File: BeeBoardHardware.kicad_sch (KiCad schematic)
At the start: 48 parts, among them J1 Conn_01x10, J2 USB_C_Receptacle_USB2.0_16P, J3 Conn_01x02, Q1 AO3413, Q2 MMBT3904, Q3 MMBT3904, SW1 SW_Push, U1 MCP16311x-xMNY, U2 BQ24074RGT, U3 USBLC6-2SC6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

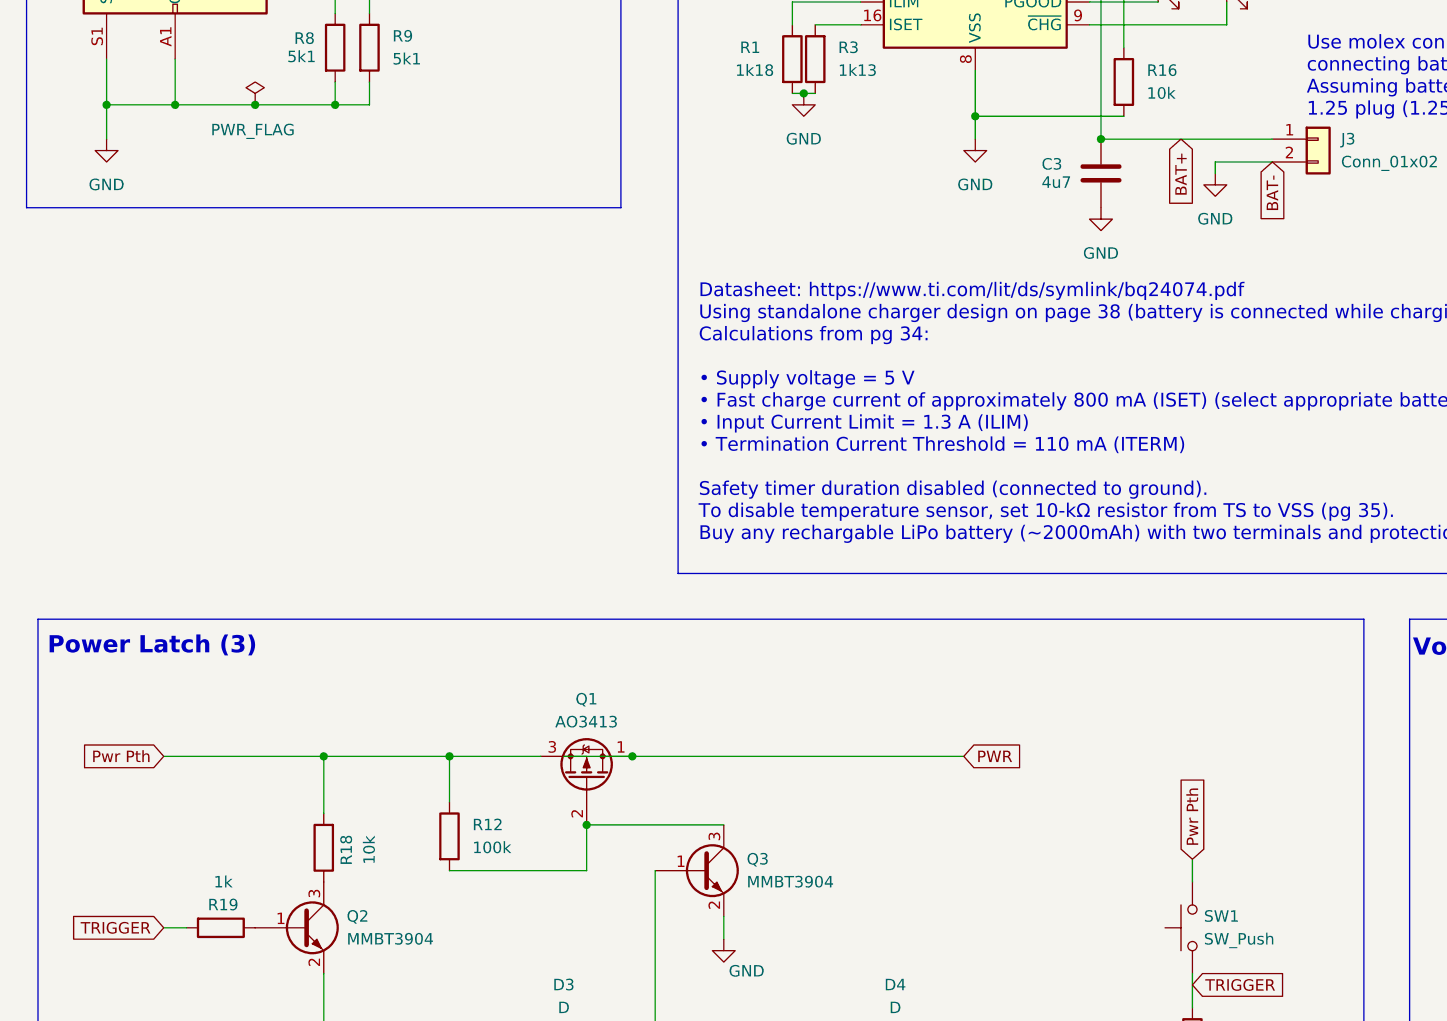
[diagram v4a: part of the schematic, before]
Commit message: updated stepper files
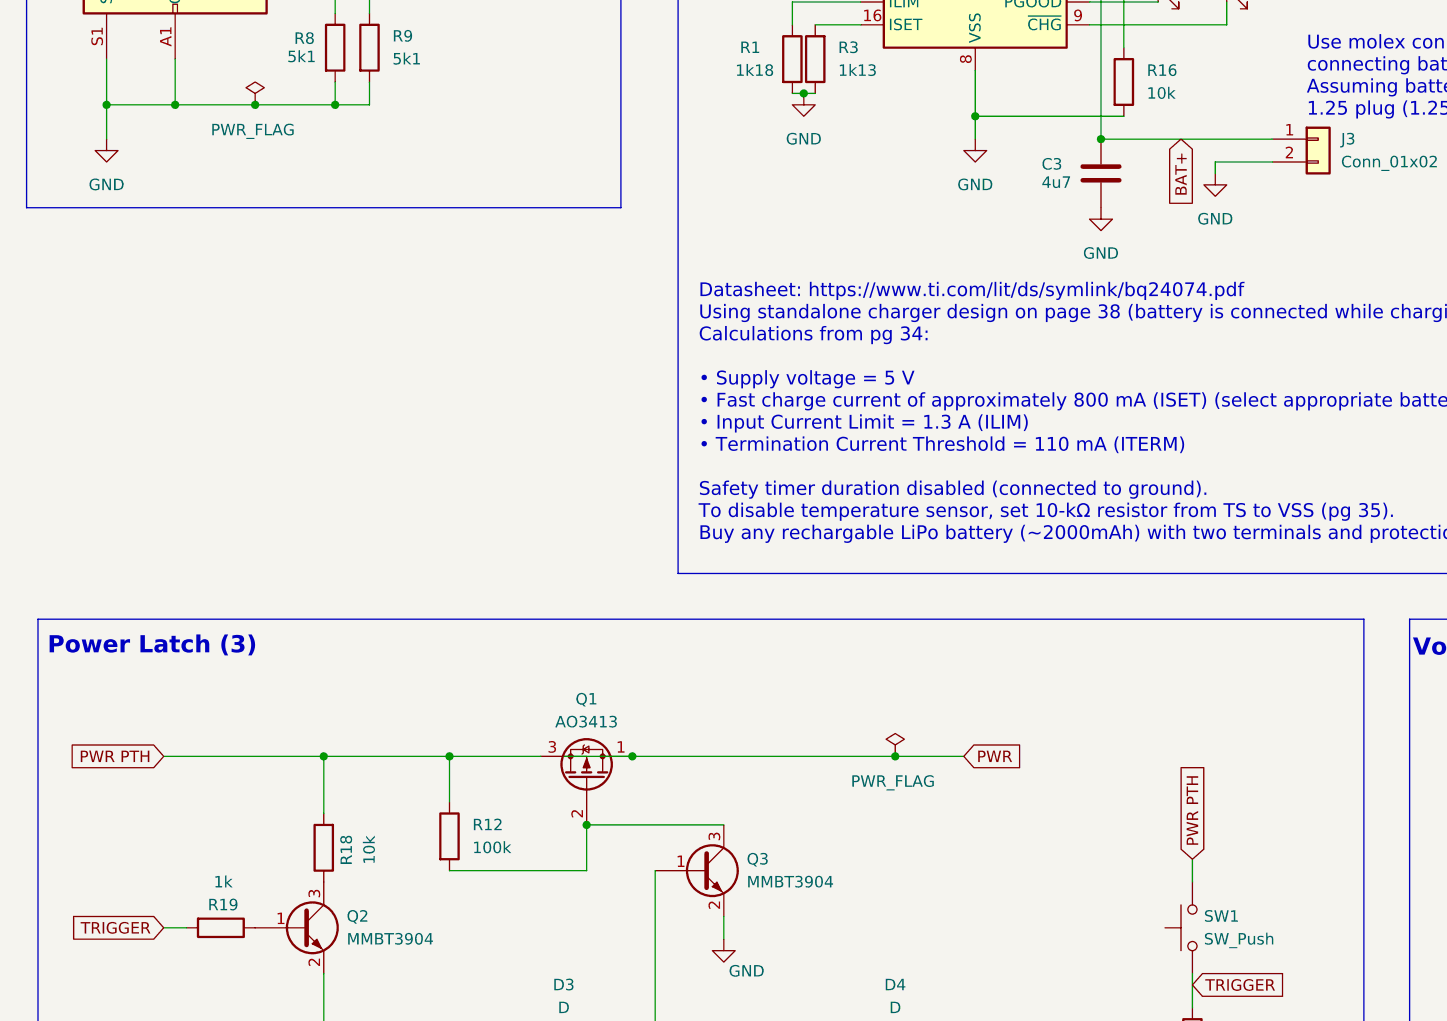
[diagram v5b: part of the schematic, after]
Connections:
- net Pwr Pth is gone; now on net PWR PTH: Q1.3 (S), R12.1, R18.2, SW1.2
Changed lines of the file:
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@@
 	)
 	(junction
+		(at 118.11 148.59)
+		(diameter 0)
+		(color 0 0 0 0)
+	)
+	(junction
 		(at 232.41 153.67)
 		(diameter 0)
@@
 	(wire
 		(pts
-			(xy 88.9 148.59) (xy 125.73 148.59)
+			(xy 88.9 148.59) (xy 118.11 148.59)
 		)
 		(stroke
@@
 	(wire
 		(pts
+			(xy 118.11 148.59) (xy 125.73 148.59)
+		)
+		(stroke
+			(width 0)
+			(type default)
+		)
+	)
+	(wire
+		(pts
 			(xy 55.88 73.66) (xy 55.88 76.2)
 		)
@@
 		)
 	)
-	(global_label "Pwr Pth"
+	(global_label "PWR PTH"
 		(shape input)
 		(at 36.83 148.59 180)
@@
 		)
 		(property "Intersheetrefs" "${INTERSHEET_REFS}"
-			(at 26.3458 148.59 0)
+			(at 25.3177 148.59 0)
 			(effects
 				(font
@@
 		)
 	)
-	(global_label "BAT-"
-		(shape input)
-		(at 160.02 82.55 270)
-		(fields_autoplaced yes)
-		(effects
-			(font
-				(size 1.27 1.27)
-			)
-			(justify right)
-		)
-		(property "Intersheetrefs" "${INTERSHEET_REFS}"
-			(at 160.02 90.4338 90)
-			(effects
-				(font
-					(size 1.27 1.27)
-				)
-				(justify right)
-				(hide yes)
-			)
-		)
-	)
 	(global_label "TRIGGER"
 		(shape input)
@@
 		)
 	)
-	(global_label "Pwr Pth"
+	(global_label "PWR PTH"
 		(shape input)
 		(at 151.13 160.02 90)
@@
 		)
 		(property "Intersheetrefs" "${INTERSHEET_REFS}"
-			(at 151.13 149.5358 90)
+			(at 151.13 148.5077 90)
 			(effects
 				(font
@@
 					(unit 1)
 				)
+			)
+		)
+	)
+	(symbol
+		(lib_id "power:PWR_FLAG")
+		(at 118.11 148.59 0)
+		(unit 1)
+		(exclude_from_sim no)
+		(in_bom yes)
+		(on_board yes)
+		(dnp no)
+		(property "Reference" "#FLG03"
+			(at 118.11 146.685 0)
+			(effects
+				(font
+					(size 1.27 1.27)
+				)
+				(hide yes)
+			)
+		)
+		(property "Value" "PWR_FLAG"
+			(at 117.856 151.384 0)
+			(effects
+				(font
+					(size 1.27 1.27)
+				)
+			)
+		)
+		(property "Footprint" ""
+			(at 118.11 148.59 0)
+			(effects
+				(font
+					(size 1.27 1.27)
+				)
+				(hide yes)
+			)
+		)
+		(property "Datasheet" "~"
+			(at 118.11 148.59 0)
+			(effects
+				(font
+					(size 1.27 1.27)
+				)
+				(hide yes)
+			)
+		)
+		(property "Description" "Special symbol for telling ERC where power comes from"
+			(at 118.11 148.59 0)
+			(effects
+				(font
+					(size 1.27 1.27)
+				)
+				(hide yes)
+			)
+		)
+		(pin "1"
+		)
+		(instances
+			(project "BeeBoardHardware"
+				(path "/e994c545-1735-4419-a83b-30b4b610da30"
+					(reference "#FLG03")
+					(unit 1)
+				)

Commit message: organized pcb
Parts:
- removed Q1: AO3413, Package_TO_SOT_SMD:SOT-23, symbol Device:Q_PMOS_DGS
- added Q4: AO3413, Package_TO_SOT_SMD:SOT-23, symbol Device:Q_PMOS_GSD
- added R21: 1k, Resistor_SMD:R_0402_1005Metric, symbol Device:R
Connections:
- net +3v3: now also R21.1
- net GND: now also R21.2
- net PWR: now also Q4.2 (S)
- net PWR PTH: now also Q4.3 (D)
- net at Q3.3 (C), R12.2: now also Q4.1 (G)
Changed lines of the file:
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@@
 	)
 	(junction
-		(at 83.82 156.21)
-		(diameter 0)
-		(color 0 0 0 0)
-	)
-	(junction
 		(at 204.47 151.13)
 		(diameter 0)
@@
 	)
 	(junction
-		(at 101.6 54.61)
+		(at 83.82 156.21)
 		(diameter 0)
 		(color 0 0 0 0)
 	)
 	(junction
-		(at 62.23 33.02)
+		(at 101.6 54.61)
 		(diameter 0)
 		(color 0 0 0 0)
 	)
 	(junction
-		(at 248.92 67.31)
+		(at 62.23 33.02)
 		(diameter 0)
 		(color 0 0 0 0)
 	)
 	(junction
-		(at 54.61 148.59)
+		(at 248.92 67.31)
 		(diameter 0)
 		(color 0 0 0 0)
 	)
 	(junction
-		(at 88.9 148.59)
+		(at 54.61 148.59)
 		(diameter 0)
 		(color 0 0 0 0)
@@
 	(wire
 		(pts
-			(xy 81.28 148.59) (xy 88.9 148.59)
-		)
-		(stroke
-			(width 0)
-			(type default)
-		)
-	)
-	(wire
-		(pts
 			(xy 193.04 151.13) (xy 204.47 151.13)
 		)
@@
 		)
 	)
+	(global_label "+3v3"
+		(shape input)
+		(at 281.94 153.67 90)
+		(fields_autoplaced yes)
+		(effects
+			(font
+				(size 1.27 1.27)
+			)
+			(justify left)
+		)
+		(property "Intersheetrefs" "${INTERSHEET_REFS}"
+			(at 281.94 145.7258 90)
+			(effects
+				(font
+					(size 1.27 1.27)
+				)
+				(justify left)
+				(hide yes)
+			)
+		)
+	)
 	(symbol
 		(lib_id "Device:D")
@@
 	)
 	(symbol
+		(lib_id "power:GND")
+		(at 281.94 161.29 0)
+		(unit 1)
+		(exclude_from_sim no)
+		(in_bom yes)
+		(on_board yes)
+		(dnp no)
+		(property "Reference" "#PWR09"
+			(at 281.94 167.64 0)
+			(effects
+				(font
+					(size 1.27 1.27)
+				)
+				(hide yes)
+			)
+		)
+		(property "Value" "GND"
+			(at 281.94 166.37 0)
+			(effects
+				(font
+					(size 1.27 1.27)
+				)
+			)
+		)
+		(property "Footprint" ""
+			(at 281.94 161.29 0)
+			(effects
+				(font
+					(size 1.27 1.27)
+				)
+				(hide yes)
+			)
+		)
+		(property "Datasheet" ""
+			(at 281.94 161.29 0)
+			(effects
+				(font
+					(size 1.27 1.27)
+				)
+				(hide yes)
+			)
+		)
+		(property "Description" "Power symbol creates a global label with name \"GND\" , ground"
+			(at 281.94 161.29 0)
+			(effects
+				(font
+					(size 1.27 1.27)
+				)
+				(hide yes)
+			)
+		)
+		(pin "1"
+		)
+		(instances
+			(project "BeeBoardHardware"
+				(path "/e994c545-1735-4419-a83b-30b4b610da30"
+					(reference "#PWR09")
+					(unit 1)
+				)
+			)
+		)
+	)
+	(symbol
 		(lib_id "Device:C")
 		(at 120.65 31.75 0)
@@
 	)
 	(symbol
+		(lib_id "Device:R")
+		(at 281.94 157.48 0)
+		(unit 1)
+		(exclude_from_sim no)
+		(in_bom yes)
+		(on_board yes)
+		(dnp no)
+		(property "Reference" "R21"
+			(at 279.4 157.226 90)
+			(effects
+				(font
+					(size 1.27 1.27)
+				)
+			)
+		)
+		(property "Value" "1k"
+			(at 276.86 157.226 90)
+			(effects
+				(font
+					(size 1.27 1.27)
+				)
+			)
+		)
+		(property "Footprint" "Resistor_SMD:R_0402_1005Metric"
+			(at 280.162 157.48 90)
+			(effects
+				(font
+					(size 1.27 1.27)
+				)
+				(hide yes)
+			)
+		)
+		(property "Datasheet" "~"
+			(at 281.94 157.48 0)
+			(effects
+				(font
+					(size 1.27 1.27)
+				)
+				(hide yes)
+			)
+		)
+		(property "Description" "Resistor"
+			(at 281.94 157.48 0)
+			(effects
+				(font
+					(size 1.27 1.27)
+				)
+				(hide yes)
+			)
+		)
+		(property "Digikey Link" ""
+			(at 281.94 157.48 0)
+			(effects
+				(font
+					(size 1.27 1.27)
+				)
+				(hide yes)
+			)
+		)
+		(property "Manufacturer Product Number" ""
+			(at 281.94 157.48 0)
+			(effects
+				(font
+					(size 1.27 1.27)
+				)
+				(hide yes)
+			)
+		)
+		(pin "1"
+		)
+		(pin "2"
+		)
+		(instances
+			(project "BeeBoardHardware"
+				(path "/e994c545-1735-4419-a83b-30b4b610da30"
+					(reference "R21")
+					(unit 1)
+				)
+			)
+		)
+	)
+	(symbol
 		(lib_id "Device:C")
 		(at 163.83 50.8 0)
@@
 	)
 	(symbol
-		(lib_id "Device:Q_PMOS_DGS")
-		(at 83.82 151.13 270)
-		(mirror x)
-		(unit 1)
-		(exclude_from_sim no)
-		(in_bom yes)
-		(on_board yes)
-		(dnp no)
-		(property "Reference" "Q1"
-			(at 83.82 142.24 90)
-			(effects
-				(font
-					(size 1.27 1.27)
-				)
-			)
-		)
-		(property "Value" "AO3413"
-			(at 83.82 144.78 90)
-			(effects
-				(font
-					(size 1.27 1.27)
-				)
-			)
-		)
-		(property "Footprint" "Package_TO_SOT_SMD:SOT-23"
-			(at 86.36 146.05 0)
-			(effects
-				(font
-					(size 1.27 1.27)
-				)
-				(hide yes)
-			)
-		)
-		(property "Datasheet" "https://www.aosmd.com/sites/default/files/res/datasheets/AO3413.pdf"
-			(at 83.82 151.13 0)
-			(effects
-				(font
-					(size 1.27 1.27)
-				)
-				(hide yes)
-			)
-		)
-		(property "Description" "P-MOSFET transistor, drain/gate/source"
-			(at 83.82 151.13 0)
-			(effects
-				(font
-					(size 1.27 1.27)
-				)
-				(hide yes)
-			)
-		)
-		(property "Digikey Link" "https://www.digikey.com/en/products/detail/alpha-omega-semiconductor-inc/AO3413/1855780"
-			(at 83.82 151.13 0)
-			(effects
-				(font
-					(size 1.27 1.27)
-				)
-				(hide yes)
-			)
-		)
-		(property "Manufacturer Product Number" "AO3413"
-			(at 83.82 151.13 0)
-			(effects
-				(font
-					(size 1.27 1.27)
-				)
-				(hide yes)
-			)
-		)
-		(pin "1"
-		)
-		(pin "2"
-		)
-		(pin "3"
-		)
-		(instances
-			(project ""
-				(path "/e994c545-1735-4419-a83b-30b4b610da30"
-					(reference "Q1")
-					(unit 1)
-				)
-			)
-		)
-	)
-	(symbol
 		(lib_id "power:PWR_FLAG")
 		(at 46.99 76.2 0)
@@
 					(unit 1)
 				)
+			)
+		)
+	)
+	(symbol
+		(lib_id "Device:Q_PMOS_GSD")
+		(at 83.82 151.13 90)
+		(unit 1)
+		(exclude_from_sim no)
+		(in_bom yes)
+		(on_board yes)
+		(dnp no)
+		(fields_autoplaced yes)
+		(property "Reference" "Q4"
+			(at 83.82 142.24 90)
+			(effects
+				(font
+					(size 1.27 1.27)
+				)
+			)
+		)
+		(property "Value" "AO3413"
+			(at 83.82 144.78 90)
+			(effects
+				(font
+					(size 1.27 1.27)
+				)
+			)
+		)
+		(property "Footprint" "Package_TO_SOT_SMD:SOT-23"
+			(at 81.28 146.05 0)
+			(effects
+				(font
+					(size 1.27 1.27)
+				)
+				(hide yes)
+			)
+		)
+		(property "Datasheet" "https://www.aosmd.com/sites/default/files/res/datasheets/AO3413.pdf"
+			(at 83.82 151.13 0)
+			(effects
+				(font
+					(size 1.27 1.27)
+				)
+				(hide yes)
+			)
+		)
+		(property "Description" "P-MOSFET transistor, gate/source/drain"
+			(at 83.82 151.13 0)
+			(effects
+				(font
+					(size 1.27 1.27)
+				)
+				(hide yes)
+			)
+		)
+		(property "Digikey Link" "https://www.digikey.com/en/products/detail/alpha-omega-semiconductor-inc/AO3413/1855780"
+			(at 83.82 151.13 0)
+			(effects
+				(font
+					(size 1.27 1.27)
+				)
+				(hide yes)
+			)
+		)
+		(property "Manufacturer Product Number" "AO3413"
+			(at 83.82 151.13 0)
+			(effects
+				(font
+					(size 1.27 1.27)
+				)
+				(hide yes)
+			)
+		)
+		(pin "3"
+		)
+		(pin "2"
+		)
+		(pin "1"
+		)
+		(instances
+			(project ""
+				(path "/e994c545-1735-4419-a83b-30b4b610da30"
+					(reference "Q4")
+					(unit 1)
+				)

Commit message: updated schematics and PCB
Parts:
- removed D3, D4: D, Diode_SMD:D_0402_1005Metric, symbol Device:D
- removed J1: Conn_01x10, Connector_PinHeader_2.54mm:PinHeader_1x10_P2.54mm_Vertical, symbol Connector_Generic:Conn_01x10
- removed Q2, Q3: MMBT3904, Package_TO_SOT_SMD:SOT-23, symbol Transistor_BJT:MMBT3904
- removed Q4: AO3413, Package_TO_SOT_SMD:SOT-23, symbol Device:Q_PMOS_GSD
- removed R11, R20: 220k, Resistor_SMD:R_0402_1005Metric, symbol Device:R
- removed R12, R14: 100k, Resistor_SMD:R_0402_1005Metric, symbol Device:R
- removed R13, R18: 10k, Resistor_SMD:R_0402_1005Metric, symbol Device:R
- removed R15: 220, Resistor_SMD:R_0402_1005Metric, symbol Device:R
- removed R19: 1k, Resistor_SMD:R_0402_1005Metric, symbol Device:R
- removed SW1: SW_Push, footprints:3983_switch, symbol Switch:SW_Push
- added C10: 470n, Capacitor_SMD:C_0402_1005Metric, symbol Device:C
- added C11: 1u, Capacitor_SMD:C_0402_1005Metric, symbol Device:C
- added C12: 10n, Capacitor_SMD:C_0402_1005Metric, symbol Device:C
- added C9: 100n, Capacitor_SMD:C_0402_1005Metric, symbol Device:C
- added D5, D7: LED, LED_SMD:LED_0402_1005Metric, symbol Device:LED
- added J4: Conn_01x11, Connector_PinHeader_2.54mm:PinHeader_1x11_P2.54mm_Vertical, symbol Connector_Generic:Conn_01x11
- added Q1: AO3413, Package_TO_SOT_SMD:SOT-23, symbol Device:Q_PMOS_GSD
- added R22: 560, Resistor_SMD:R_0402_1005Metric, symbol Device:R
- added R23: 10k, Resistor_SMD:R_0402_1005Metric, symbol Device:R
- added SW2: SW_Push, footprints:3983_switch, symbol Switch:SW_Push
- added U5: STM6600DQ25DM6F, Package_DFN_QFN:TDFN-12_2x3mm_P0.5mm, symbol Power_Management:STM6600
- R21: value 1k -> 10k
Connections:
- net +3v3: now also D5.2 (A), J4.1 (Pin_1); no longer R21.1
- net BAT_ALERT: now also J4.2 (Pin_2)
- net BAT_SCL: now also J4.4 (Pin_4)
- net BAT_SDA: now also J4.3 (Pin_3)
- net GND: now also C10.2, C11.2, C12.2, C9.2, D5.1 (K), J4.11 (Pin_11), SW2.1, U5.12 (GND); no longer R21.2
- net LATCH: now also J4.8 (Pin_8), U5.4 (PS_HOLD)
- net PWR: now also Q1.3 (D)
- net PWR PTH: now also R21.2, C9.1, D7.2 (A), Q1.2 (S), R23.2, U5.1 (Vcc)
- net USB_D+: now also J4.6 (Pin_6)
- net USB_D-: now also J4.5 (Pin_5)
- net VBUS: now also J4.7 (Pin_7)
- new net: C11.1, U5.3 (Vref)
- new net: C12.1, SW2.2, U5.2 (~{SR}), U5.6 (~{PB})
- new net: C10.1, U5.5 (C_SRD)
- new net: Q1.1 (G), R23.1, U5.9 (~{EN}/EN)
- new net: R22.1, U5.7 (~{VCC}_LO)
- new net: R21.1, U5.8 (~{PB}_OUT)
- new net: D7.1 (K), R22.2
- new net PWR_DOWN: J4.9 (Pin_9), U5.11 (~{INT})
- new net RST: J4.10 (Pin_10), U5.10 (~{RST})
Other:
- note added: "App Notes: https://www.st.com/resource/en/application_note/ an3271-using-the-stm6600-stm6601-smart-pushbutton-onoff-controller-stmicroelectronics.pdf Breakout Board: https://www.st.com/resource/en/schematic_pack/stdes-stm660-schematic.pdf Datasheet: https://www.st.com/resource/en/datasheet/stm6600.pdf ● If the device is off, press the push-button to power up (MCU must enable PS_HOLD to maintain p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"
- note added: "Datasheet: https://www.digikey.com/en/products/detail/ onsemi/LC709203FQH-01TWG/4847843 For LC709203Fxx−01xx, we have two profiles available. We want to use battery type 01 (pg 13) for our single cell LiPo 2000mAh w/ nominal 3v7."
- note added: "Exlanations for headers: 1) +3v3: regulated output voltage 2) BAT_ALERT: interrupt from battery moniter 3) BAT_SDA: I2C for battery moniter 4) BAT_SCL: I2C for battery moniter 5) USB_D-: dataline 6) USB_D+: dataline 7) VBUS: USB bus 8) LATCH: GPIO to programtically turn off power 9) PWR_DOWN: external signal to power down (due to low battery or button) 10) RST: external signal to reset 11) GND: r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"
- note added: "Power Button (#3)"
- note removed: "Datasheet available (Google)"
- note removed: "Exlanations for headers: 1) +3v3: regulated output voltage 2) BAT_ALERT: interrupt from battery moniter 3) BAT_SDA: I2C for battery moniter 4) BAT_SCL: I2C for battery moniter 5) USB_D-: dataline 6) USB_D+: dataline 7) VBUS: USB bus 8) LATCH: GPIO to programtically turn off power 9) TRIGGER: manual power button to turn on/off power 10) GND: reference ground"
- note removed: "Power Latch (3)"
- note removed: "Reference circuits: 1) https://randomnerdtutorials.com/latching-power-switch-circuit-auto-power-off-circuit-esp32-esp8266-arduino/ 2) https://randomnerdtutorials.com/power-saving-latching-circuit/"
- moved on the sheet: C1, C2, C3, C4, C5, C6, C7, C8, D1, D2, H1, H2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
